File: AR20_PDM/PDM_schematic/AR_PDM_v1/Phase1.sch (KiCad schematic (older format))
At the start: 10 parts, among them Q1 BTS50025-1TAD, U2 INA233

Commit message: Working on pcb layout
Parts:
- removed D?: D_Schottky_x2, symbol AR20_PDM_v1-rescue:D_Schottky_x2
- added D2, D4: D_Schottky_BAT60A, AR_PDM_v1:D_Shotky_BAT60_HandSoldering, symbol AR20_PDM_v1-rescue:D_Schottky_BAT60A
- gave numbers to parts that had none: 3
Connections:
- net GND: now also D2.2 (A), D4.2 (A)
- net at R12.1, U2.10 (IN+): now also D4.1 (K)
- net at R11.1, U2.9 (In-): now also D2.1 (K)
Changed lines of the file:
@@
 V+12V
 $Comp
-L AR20_PDM_v1-rescue:D_Schottky_x2 D?
-U 1 1 5EEF7119
-P 6950 4825
-F 0 "D?" H 6950 5041 50  0000 C CNN
-F 1 "D_Schottky_x2" H 6950 4950 50  0000 C CNN
-F 2 "" H 6950 4825 50  0001 C CNN
-F 3 "~" H 6950 4825 50  0001 C CNN
-	1    6950 4825
-	1    0    0    -1
-$EndComp
-$Comp
-L AR20_PDM_v1-rescue:R-Device R?
+L AR20_PDM_v1-rescue:R-Device R11
 U 1 1 5EEFC1FD
 P 6650 3850
-AR Path="/5DA89415/5EEFC1FD" Ref="R?"  Part="1"
+AR Path="/5DA89415/5EEFC1FD" Ref="R11"  Part="1"
 AR Path="/5DEB10A1/5EEFC1FD" Ref="R?"  Part="1"
 AR Path="/5DEB20EA/5EEFC1FD" Ref="R?"  Part="1"
@@
 AR Path="/5E0FDCCC/5EEFC1FD" Ref="R?"  Part="1"
 AR Path="/5E10174B/5EEFC1FD" Ref="R?"  Part="1"
-F 0 "R?" V 6443 3850 50  0000 C CNN
+F 0 "R11" V 6443 3850 50  0000 C CNN
 F 1 "1K_1%" V 6534 3850 50  0000 C CNN
 F 2 "Resistor_SMD:R_0603_1608Metric" V 6580 3850 50  0001 C CNN
@@
 $EndComp
 $Comp
-L AR20_PDM_v1-rescue:R-Device R?
+L AR20_PDM_v1-rescue:R-Device R12
 U 1 1 5EEFCB85
 P 7050 3850
-AR Path="/5DA89415/5EEFCB85" Ref="R?"  Part="1"
+AR Path="/5DA89415/5EEFCB85" Ref="R12"  Part="1"
 AR Path="/5DEB10A1/5EEFCB85" Ref="R?"  Part="1"
 AR Path="/5DEB20EA/5EEFCB85" Ref="R?"  Part="1"
@@
 AR Path="/5E0FDCCC/5EEFCB85" Ref="R?"  Part="1"
 AR Path="/5E10174B/5EEFCB85" Ref="R?"  Part="1"
-F 0 "R?" V 6843 3850 50  0000 C CNN
+F 0 "R12" V 6843 3850 50  0000 C CNN
 F 1 "1K_1%" V 6934 3850 50  0000 C CNN
 F 2 "Resistor_SMD:R_0603_1608Metric" V 6980 3850 50  0001 C CNN
@@
 Text Notes 7075 2000 0    50   ~ 10
 Place shunt and INA233 close, \nroute togethere, differentialy pair. \nKeep short, and away from Noise.
-$Comp
-L AR20_PDM_v1-rescue:GND-power #PWR?
-U 1 1 5EF15BFC
-P 6950 5025
-AR Path="/5DA89415/5EF15BFC" Ref="#PWR?"  Part="1"
-AR Path="/5DEB10A1/5EF15BFC" Ref="#PWR?"  Part="1"
-AR Path="/5DEB20EA/5EF15BFC" Ref="#PWR?"  Part="1"
-AR Path="/5E0E4725/5EF15BFC" Ref="#PWR?"  Part="1"
-AR Path="/5E0E4A93/5EF15BFC" Ref="#PWR?"  Part="1"
-AR Path="/5E0E4EB5/5EF15BFC" Ref="#PWR?"  Part="1"
-AR Path="/5E0E5304/5EF15BFC" Ref="#PWR?"  Part="1"
-AR Path="/5E0E594B/5EF15BFC" Ref="#PWR?"  Part="1"
-AR Path="/5E0E607C/5EF15BFC" Ref="#PWR?"  Part="1"
-AR Path="/5E0FB5C8/5EF15BFC" Ref="#PWR?"  Part="1"
-AR Path="/5E0FBBBD/5EF15BFC" Ref="#PWR?"  Part="1"
-AR Path="/5E0FC3A2/5EF15BFC" Ref="#PWR?"  Part="1"
-AR Path="/5E0FCFDC/5EF15BFC" Ref="#PWR?"  Part="1"
-AR Path="/5E0FDCCC/5EF15BFC" Ref="#PWR?"  Part="1"
-AR Path="/5E10174B/5EF15BFC" Ref="#PWR?"  Part="1"
-F 0 "#PWR?" H 6950 4775 50  0001 C CNN
-F 1 "GND" H 6955 4852 50  0000 C CNN
-F 2 "" H 6950 5025 50  0001 C CNN
-F 3 "" H 6950 5025 50  0001 C CNN
-	1    6950 5025
-	1    0    0    -1
-$EndComp
 Text HLabel 8150 4100 0    50   Output ~ 10
 P1_OUT
 $Comp
-L AR20_PDM_v1-rescue:R-Device R?
+L AR20_PDM_v1-rescue:R-Device R15
 U 1 1 5EF1BC51
 P 8300 4100
-AR Path="/5DA89415/5EF1BC51" Ref="R?"  Part="1"
+AR Path="/5DA89415/5EF1BC51" Ref="R15"  Part="1"
 AR Path="/5DEB10A1/5EF1BC51" Ref="R?"  Part="1"
 AR Path="/5DEB20EA/5EF1BC51" Ref="R?"  Part="1"
@@
 AR Path="/5E0FDCCC/5EF1BC51" Ref="R?"  Part="1"
 AR Path="/5E10174B/5EF1BC51" Ref="R?"  Part="1"
-F 0 "R?" V 8093 4100 50  0000 C CNN
+F 0 "R15" V 8093 4100 50  0000 C CNN
 F 1 "10K" V 8184 4100 50  0000 C CNN
 F 2 "Resistor_SMD:R_0603_1608Metric" V 8230 4100 50  0001 C CNN
@@
 Wire Wire Line
 	6650 4400 8750 4400
+Wire Wire Line
+	7050 4300 7100 4300
+$Comp
+L AR20_PDM_v1-rescue:D_Schottky_BAT60A D2
+U 1 1 5EF91750
+P 6700 4775
+F 0 "D2" V 6530 4885 50  0000 L CNN
+F 1 "D_Schottky_BAT60A" V 6621 4885 50  0000 L CNN
+F 2 "AR_PDM_v1:D_Shotky_BAT60_HandSoldering" H 6800 4725 50  0001 C CNN
+F 3 "~" H 6800 4725 50  0001 C CNN
+	1    6700 4775
+	0    1    1    0
+$EndComp
+$Comp
+L AR20_PDM_v1-rescue:GND-power #PWR0168
+U 1 1 5EF15BFC
+P 6875 4950
+AR Path="/5DA89415/5EF15BFC" Ref="#PWR0168"  Part="1"
+AR Path="/5DEB10A1/5EF15BFC" Ref="#PWR?"  Part="1"
+AR Path="/5DEB20EA/5EF15BFC" Ref="#PWR?"  Part="1"
+AR Path="/5E0E4725/5EF15BFC" Ref="#PWR?"  Part="1"
+AR Path="/5E0E4A93/5EF15BFC" Ref="#PWR?"  Part="1"
+AR Path="/5E0E4EB5/5EF15BFC" Ref="#PWR?"  Part="1"
+AR Path="/5E0E5304/5EF15BFC" Ref="#PWR?"  Part="1"
+AR Path="/5E0E594B/5EF15BFC" Ref="#PWR?"  Part="1"
+AR Path="/5E0E607C/5EF15BFC" Ref="#PWR?"  Part="1"
+AR Path="/5E0FB5C8/5EF15BFC" Ref="#PWR?"  Part="1"
+AR Path="/5E0FBBBD/5EF15BFC" Ref="#PWR?"  Part="1"
+AR Path="/5E0FC3A2/5EF15BFC" Ref="#PWR?"  Part="1"
+AR Path="/5E0FCFDC/5EF15BFC" Ref="#PWR?"  Part="1"
+AR Path="/5E0FDCCC/5EF15BFC" Ref="#PWR?"  Part="1"
+AR Path="/5E10174B/5EF15BFC" Ref="#PWR?"  Part="1"
+F 0 "#PWR0168" H 6875 4700 50  0001 C CNN
+F 1 "GND" H 6880 4777 50  0000 C CNN
+F 2 "" H 6875 4950 50  0001 C CNN
+F 3 "" H 6875 4950 50  0001 C CNN
+	1    6875 4950
+	1    0    0    -1
+$EndComp
+$Comp
+L AR20_PDM_v1-rescue:D_Schottky_BAT60A D4
+U 1 1 5EF9763A
+P 7150 4775
+F 0 "D4" V 6980 4885 50  0000 L CNN
+F 1 "D_Schottky_BAT60A" V 7071 4885 50  0000 L CNN
+F 2 "AR_PDM_v1:D_Shotky_BAT60_HandSoldering" H 7250 4725 50  0001 C CNN
+F 3 "~" H 7250 4725 50  0001 C CNN
+	1    7150 4775
+	0    1    1    0
+$EndComp
+Wire Wire Line
+	6650 4475 6650 4400
 Connection ~ 6650 4400
 Wire Wire Line
-	6650 4400 6650 4825
+	7100 4475 7100 4300
+Connection ~ 7100 4300
 Wire Wire Line
-	8750 4300 7250 4300
+	7100 4300 8750 4300
 Wire Wire Line
-	7250 4825 7250 4300
-Connection ~ 7250 4300
+	6650 4825 6875 4825
 Wire Wire Line
-	7250 4300 7050 4300
+	6875 4950 6875 4825
+Connection ~ 6875 4825
+Wire Wire Line
+	6875 4825 7100 4825
 $EndSCHEMATC

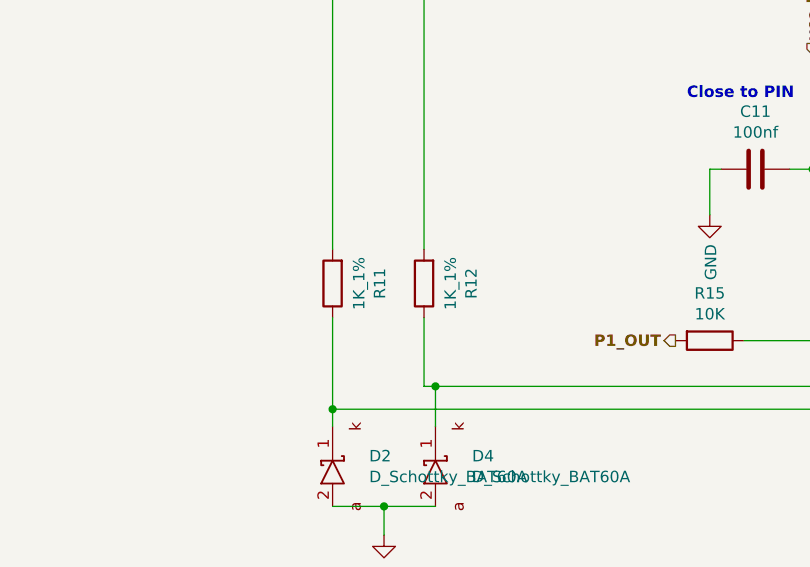
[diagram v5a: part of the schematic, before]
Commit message: shematics adjustments, and fixing values and names
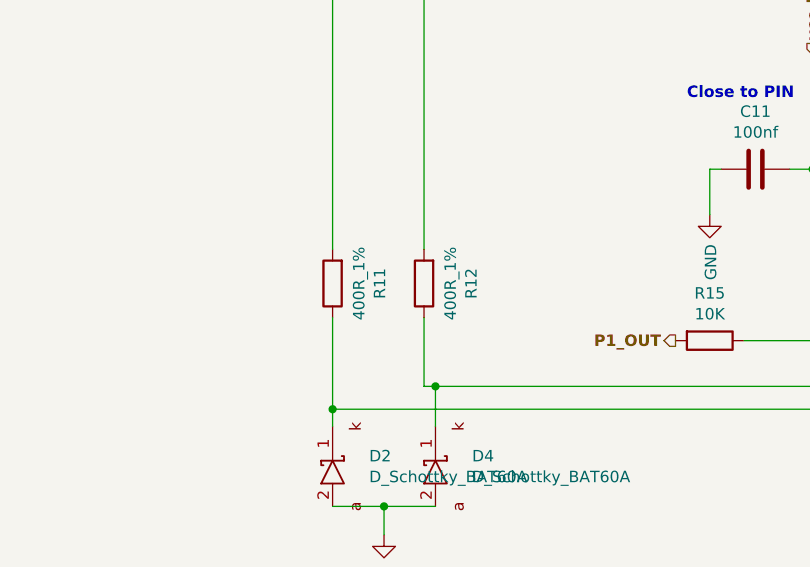
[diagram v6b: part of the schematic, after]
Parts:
- R11, R12: value 1K_1% -> 400R_1%
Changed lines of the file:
@@
 AR Path="/5E10174B/5EEFC1FD" Ref="R?"  Part="1"
 F 0 "R11" V 6443 3850 50  0000 C CNN
-F 1 "1K_1%" V 6534 3850 50  0000 C CNN
+F 1 "400R_1%" V 6534 3850 50  0000 C CNN
 F 2 "Resistor_SMD:R_0603_1608Metric" V 6580 3850 50  0001 C CNN
 F 3 "~" H 6650 3850 50  0001 C CNN
@@
 AR Path="/5E10174B/5EEFCB85" Ref="R?"  Part="1"
 F 0 "R12" V 6843 3850 50  0000 C CNN
-F 1 "1K_1%" V 6934 3850 50  0000 C CNN
+F 1 "400R_1%" V 6934 3850 50  0000 C CNN
 F 2 "Resistor_SMD:R_0603_1608Metric" V 6980 3850 50  0001 C CNN
 F 3 "~" H 7050 3850 50  0001 C CNN
